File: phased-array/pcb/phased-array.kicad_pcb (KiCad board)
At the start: 4 copper layers, 32 x 45 mm, 36 parts, among them J101 CONN_01X02, J102 CONN_01X02, J103 CONN_01X02, J104 CONN_01X02, J105 CONN_01X02, J106 CONN_01X04, U201 PCA9534A, U202 PE44820, U301 PCA9534A, U302 PE44820, U401 PD2328J, U402 PD2328J, U403 PD2328J, U501 PCA9534A, U502 PE44820, U601 PCA9534A, U602 PE44820

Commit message: route board v1
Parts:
- moved R602 120.1 mm to (113.2, 147.2), turned to 180 degrees
- moved R302 119.0 mm to (113.3, 124.2), turned to 180 degrees
- moved R601 115.7 mm to (113.3, 145.5)
- moved R301 114.6 mm to (113.2, 122.3)
- moved C301 97.7 mm to (126.4, 146.0)
- moved C601 93.0 mm to (126.4, 134.0)
- moved R501 87.0 mm to (111.4, 131.9), turned to 270 degrees
- moved R502 81.0 mm to (113.3, 131.9), turned to 90 degrees
- moved C501 75.7 mm to (121.9, 110.7)
- moved R201 63.8 mm to (113.9, 115.0), turned to 180 degrees
- moved C201 43.9 mm to (126.5, 121.9)
- moved R202 2.24 mm to (108.0, 120.1)
- moved R402 1.89 mm to (110.0, 146.6)
- moved U402 1.80 mm to (107.5, 146.5)
- moved C302 0.82 mm to (114.0, 128.4)
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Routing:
- net GND: track 0.00 -> 206.9 mm, vias 0 -> 258
- net /SCL: track 0.00 -> 64.2 mm, vias 0 -> 3
- net /SDA: track 0.00 -> 62.0 mm, vias 0 -> 3
- net +3V3: track 0.00 -> 37.1 mm, vias 0 -> 18
- net Net-(U201-Pad10): track 0.00 -> 21.4 mm
- net Net-(U201-Pad9): track 0.00 -> 19.5 mm
- net Net-(U201-Pad8): track 0.00 -> 15.8 mm
- net Net-(U201-Pad7): track 0.00 -> 14.5 mm
- net Net-(U201-Pad5): track 0.00 -> 12.7 mm
- net Net-(U201-Pad4): track 0.00 -> 11.0 mm
- net Net-(U201-Pad3): track 0.00 -> 10.4 mm
- net /RF_4: track 0.00 -> 10.1 mm
- net /RF_2: track 0.00 -> 10.1 mm
- net /RF_1: track 0.00 -> 9.97 mm
- net Net-(U201-Pad2): track 0.00 -> 9.54 mm
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- added copper zone on F.Cu, net GND
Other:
- board size 32 x 45 mm -> 32 x 47 mm

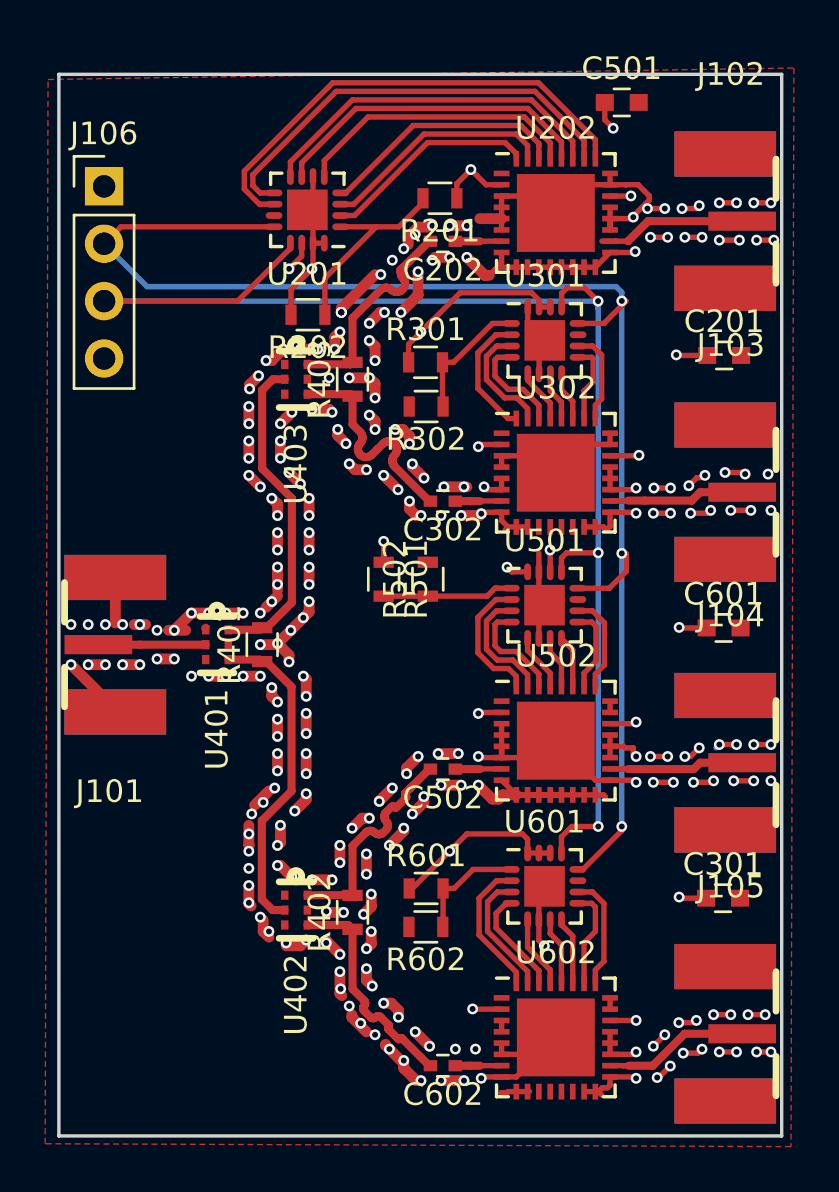
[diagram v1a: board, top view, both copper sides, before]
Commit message: phase shift board ready for fab
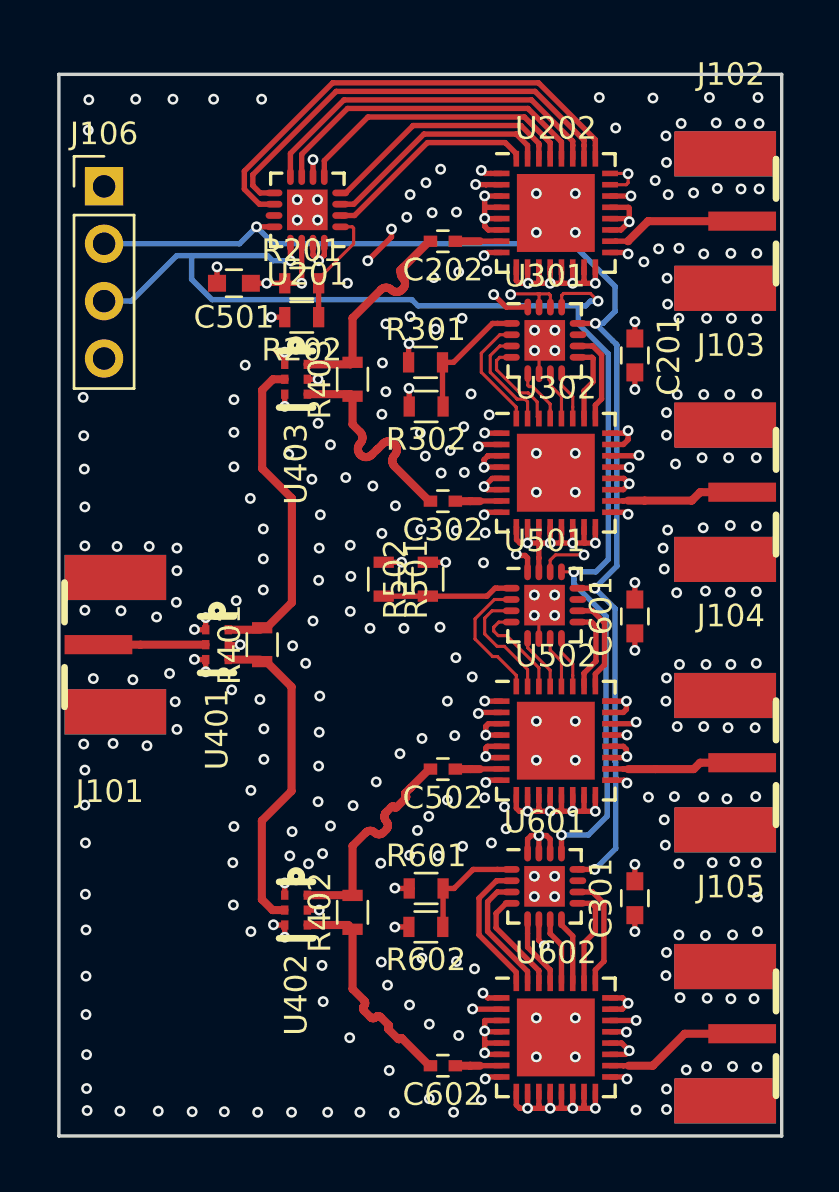
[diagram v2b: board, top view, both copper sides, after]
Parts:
- moved C501 18.9 mm to (104.8, 118.8), turned to 180 degrees
- moved R201 7.18 mm to (107.8, 118.8), turned to 0 degrees
- moved C601 3.96 mm to (122.5, 133.5), turned to 90 degrees
- moved C201 3.95 mm to (122.5, 121.9), turned to 270 degrees
- moved C301 3.90 mm to (122.5, 146.0), turned to 90 degrees
- moved R202 0.30 mm to (107.8, 120.2)
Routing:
- net GND: track 206.9 -> 535.8 mm, vias 258 -> 349
- net +3V3: track 37.1 -> 27.3 mm, vias 18 -> 20
- net /SCL: track 64.2 -> 55.5 mm, vias 3 -> 4
- net /phase shifter 1/A2: track 9.12 -> 5.18 mm
- net /SDA: track 62.0 -> 60.8 mm, vias 3 -> 4
- net /RF_OUT_1: track 6.58 -> 5.99 mm
- added copper zone on B.Cu, net GND
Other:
- rule pad_to_mask_clearance: 0.2 -> 0.0635

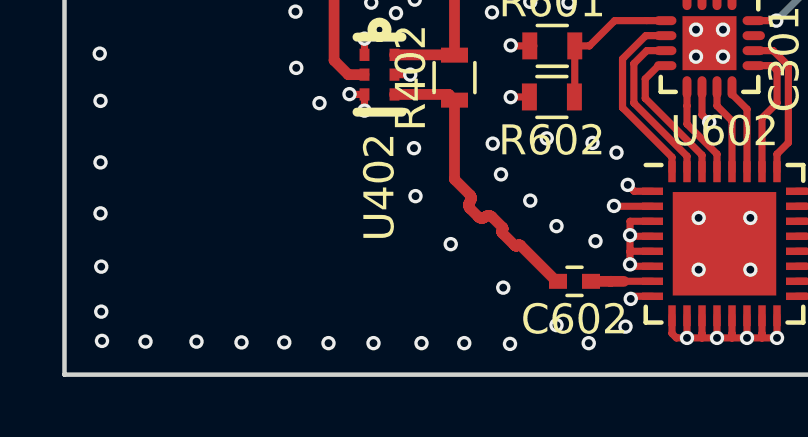
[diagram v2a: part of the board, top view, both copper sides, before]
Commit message: added PA board
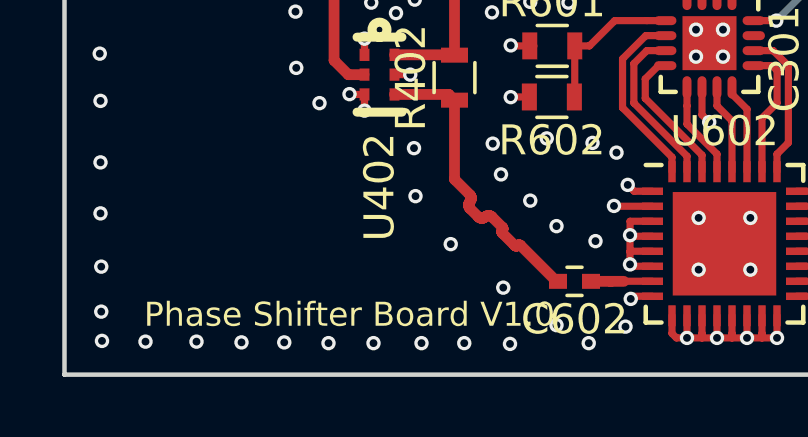
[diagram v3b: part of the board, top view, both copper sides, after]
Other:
- board text added: "Phase Shifter Board V1.0"
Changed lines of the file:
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@@
     (links 250)
     (no_connects 0)
-    (area 96.924999 109.424999 129.075001 156.575001)
+    (area 94.028667 108.587 130.971334 160.488)
     (thickness 1.6)
-    (drawings 4)
+    (drawings 5)
     (tracks 1675)
     (zones 0)
@@
     (35 F.Paste user hide)
     (36 B.SilkS user hide)
-    (37 F.SilkS user hide)
+    (37 F.SilkS user)
     (38 B.Mask user)
     (39 F.Mask user)
@@
   )
   (setup
-    (last_trace_width 0.24)
+    (last_trace_width 0.138)
     (user_trace_width 0.14)
     (user_trace_width 0.24)
@@
     (visible_elements FFFFFF7F)
     (pcbplotparams
-      (layerselection 0x00030_80000001)
-      (usegerberextensions false)
+      (layerselection 0x010f0_80000007)
+      (usegerberextensions true)
       (excludeedgelayer true)
       (linewidth 0.100000)
@@
       (psnegative false)
       (psa4output false)
-      (plotreference true)
-      (plotvalue true)
+      (plotreference false)
+      (plotvalue false)
       (plotinvisibletext false)
       (padsonsilk false)
@@
       (outputformat 1)
       (mirror false)
-      (drillshape 1)
+      (drillshape 0)
       (scaleselection 1)
-      (outputdirectory ""))
+      (outputdirectory ../../phased-array-gerbers/))
   )
   (net 0 "")
@@
     )
   )
+  (gr_text "Phase Shifter Board V1.0\n" (at 106.5 154.5) (layer F.SilkS)
+    (effects (font (size 0.8 0.8) (thickness 0.2)))
+  )
   (gr_line (start 97 156.5) (end 97 109.5) (layer Edge.Cuts) (width 0.15))
